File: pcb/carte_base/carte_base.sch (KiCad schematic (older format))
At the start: 40 parts, among them J1 Conn_01x04, J2 Conn_01x02, J3 Conn_01x02, J4 Conn_01x02, SW1 FSMRA3JH04, U1 STM32L031, U2 DAC7563T, U3 TS9222IDT

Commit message: Carte base finie
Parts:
- removed R10, R11, R12, R13, R8, R9: 1K, Resistor_SMD:R_1206_3216Metric_Pad1.42x1.75mm_HandSolder, symbol Device:R
- removed U2: DAC7563T, Package_SO:VSSOP-10_3x3mm_P0.5mm, symbol Insa:DAC7563T
- removed U3: TS9222IDT, Package_SO:SO-8_3.9x4.9mm_P1.27mm, symbol Insa:TS9222IDT
- added C15, C16, C17, C18: 22nF, Capacitor_SMD:C_1206_3216Metric_Pad1.42x1.75mm_HandSolder, symbol Device:C
- added J5: Conn_01x02, Insa:DF3A-2P-2DS, symbol Connector_Generic:Conn_01x02
- added RN1, RN3: 1K, Resistor_SMD:R_Array_Convex_4x1206, symbol Device:R_Pack04
- added RN2: 100, Resistor_SMD:R_Array_Convex_4x1206, symbol Device:R_Pack04
- added RN4: 2.4K, Resistor_SMD:R_Array_Convex_4x1206, symbol Device:R_Pack04
- added U2: DAC7554, Package_SO:MSOP-10_3x3mm_P0.5mm, symbol Insa:DAC7554
- added U3: TS9224IDT, Package_SO:SOIC-14_3.9x8.7mm_P1.27mm, symbol Insa:TS9224IDT
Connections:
- net labels added: 10V_Inclinaison_Pos, 10V_Inclinaison_VA, 10V_Rotation_Pos, 10V_Rotation_VA, Consigne_10V_Arriere, Consigne_10V_Avant, Vdrive
- net labels removed: Analog_12V_Inclinaison, Analog_12V_Rotation, Consigne_12V_Arriere, Consigne_12V_Avant, ~DAC_CLEAR
- wire segments 129 -> 184
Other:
- note added: "Connectique"
- note added: "Entrées analogiques et mise à l'echelle (0-3,3V)"
- note added: "Filtrage alimentation"
- note added: "Nucleo-L031"
- note added: "Sorties analogiques et mise à l'echelle (0-10V)"
- moved on the sheet: C1, C13, C14, C2, C3, C7, C8, D1, J1, J2, J3, J4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

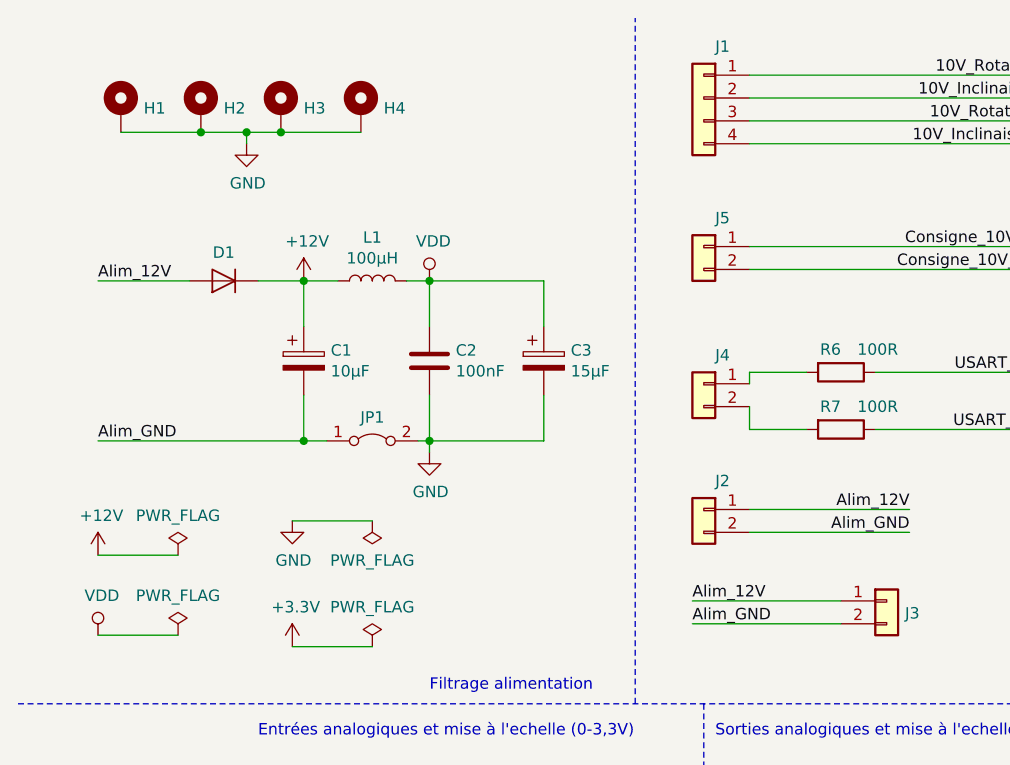
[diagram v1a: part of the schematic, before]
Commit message: Correction sur carte base
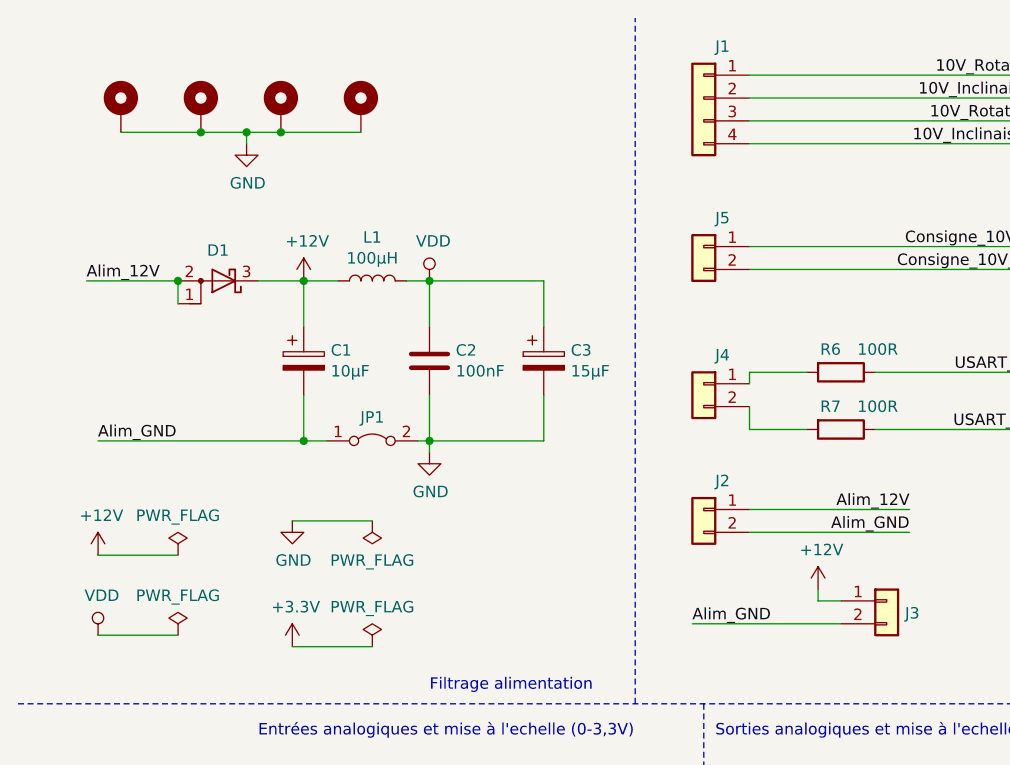
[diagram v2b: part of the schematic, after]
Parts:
- removed D1: D, Diode_SMD:D_SOD-123, symbol Device:D
- added D1: D_Schottky_AAK, Package_TO_SOT_SMD:TO-277A, symbol Device:D_Schottky_AAK
- RN1, RN2, RN3, RN4: footprint Resistor_SMD:R_Array_Convex_4x1206 -> Resistor_SMD:R_Array_Convex_4x0603
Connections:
- net +12V: now also J3.1 (Pin_1), D1.3 (K)
- net Alim_12V: now also D1.1 (A), D1.2 (A); no longer J3.1 (Pin_1)
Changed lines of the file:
@@
 U 1 1 5D2F2658
 P 950 900
-F 0 "H1" H 1050 905 50  0000 L CNN
+F 0 "H1" H 1050 905 50  0001 L CNN
 F 1 "MountingHole_Pad" H 1050 860 50  0001 L CNN
 F 2 "MountingHole:MountingHole_3.2mm_M3_ISO14580_Pad" H 950 900 50  0001 C CNN
@@
 U 1 1 5D2F26FB
 P 1300 900
-F 0 "H2" H 1400 905 50  0000 L CNN
+F 0 "H2" H 1400 905 50  0001 L CNN
 F 1 "MountingHole_Pad" H 1400 860 50  0001 L CNN
 F 2 "MountingHole:MountingHole_3.2mm_M3_ISO14580_Pad" H 1300 900 50  0001 C CNN
@@
 U 1 1 5D2F2813
 P 1650 900
-F 0 "H3" H 1750 905 50  0000 L CNN
+F 0 "H3" H 1750 905 50  0001 L CNN
 F 1 "MountingHole_Pad" H 1750 860 50  0001 L CNN
 F 2 "MountingHole:MountingHole_3.2mm_M3_ISO14580_Pad" H 1650 900 50  0001 C CNN
@@
 U 1 1 5D2F288E
 P 2000 900
-F 0 "H4" H 2100 905 50  0000 L CNN
+F 0 "H4" H 2100 905 50  0001 L CNN
 F 1 "MountingHole_Pad" H 2100 860 50  0001 L CNN
 F 2 "MountingHole:MountingHole_3.2mm_M3_ISO14580_Pad" H 2000 900 50  0001 C CNN
@@
 $EndComp
 Connection ~ 2300 1650
-Text Label 850  1650 0    50   ~ 0
+Text Label 800  1650 0    50   ~ 0
 Alim_12V
 Text Label 850  2350 0    50   ~ 0
@@
 $EndComp
 $Comp
-L Device:D D1
-U 1 1 5D8D967B
-P 1400 1650
-F 0 "D1" H 1400 1526 50  0000 C CNN
-F 1 "D" H 1400 1525 50  0001 C CNN
-F 2 "Diode_SMD:D_SOD-123" H 1400 1650 50  0001 C CNN
-F 3 "~" H 1400 1650 50  0001 C CNN
-	1    1400 1650
-	-1   0    0    1
-$EndComp
-$Comp
 L Device:CP C3
 U 1 1 5D8DE5DD
@@
 	1    0    0    -1
 $EndComp
-Wire Wire Line
-	3450 3050 4100 3050
-Text Label 3450 3050 0    50   ~ 0
-Alim_12V
 Wire Wire Line
 	4100 3150 3450 3150
@@
 DAC_DATA
 Wire Wire Line
-	1250 1650 850  1650
+	1200 1650 800  1650
 Wire Wire Line
 	1550 1650 1750 1650
@@
 F 0 "RN1" V 4883 4950 50  0000 C CNN
 F 1 "1K" V 4974 4950 50  0000 C CNN
-F 2 "Resistor_SMD:R_Array_Convex_4x1206" V 5575 4950 50  0001 C CNN
+F 2 "Resistor_SMD:R_Array_Convex_4x0603" V 5575 4950 50  0001 C CNN
 F 3 "~" H 5300 4950 50  0001 C CNN
 F 4 "CAY16-102J4AS" V 5300 4950 50  0001 C CNN "Ref"
@@
 F 0 "RN2" V 8983 5000 50  0000 C CNN
 F 1 "100" V 9074 5000 50  0000 C CNN
-F 2 "Resistor_SMD:R_Array_Convex_4x1206" V 9675 5000 50  0001 C CNN
+F 2 "Resistor_SMD:R_Array_Convex_4x0603" V 9675 5000 50  0001 C CNN
 F 3 "~" H 9400 5000 50  0001 C CNN
 F 4 "CAY16-101J4AS" V 9400 5000 50  0001 C CNN "Ref"
@@
 F 0 "RN3" H 6650 5850 50  0000 L CNN
 F 1 "1K" H 6700 5750 50  0000 L CNN
-F 2 "Resistor_SMD:R_Array_Convex_4x1206" V 7375 5750 50  0001 C CNN
+F 2 "Resistor_SMD:R_Array_Convex_4x0603" V 7375 5750 50  0001 C CNN
 F 3 "~" H 7100 5750 50  0001 C CNN
 F 4 "CAY16-102J4AS" V 7100 5750 50  0001 C CNN "Ref"
@@
 F 0 "RN4" V 8200 6150 50  0000 C CNN
 F 1 "2.4K" V 8300 6150 50  0000 C CNN
-F 2 "Resistor_SMD:R_Array_Convex_4x1206" V 8275 6150 50  0001 C CNN
+F 2 "Resistor_SMD:R_Array_Convex_4x0603" V 8275 6150 50  0001 C CNN
 F 3 "~" H 8000 6150 50  0001 C CNN
 F 4 "YC164-FR-072K4L" V 8000 6150 50  0001 C CNN "Ref"
@@
 Wire Wire Line
 	7450 4450 7550 4450
+$Comp
+L power:+12V #PWR0130
+U 1 1 5D9C510B
+P 4000 3000
+F 0 "#PWR0130" H 4000 2850 50  0001 C CNN
+F 1 "+12V" H 4015 3173 50  0000 C CNN
+F 2 "" H 4000 3000 50  0001 C CNN
+F 3 "" H 4000 3000 50  0001 C CNN
+	1    4000 3000
+	1    0    0    -1
+$EndComp
+Wire Wire Line
+	4100 3050 4000 3050
+Wire Wire Line
+	4000 3050 4000 3000
+$Comp
+L Device:D_Schottky_AAK D1
+U 1 1 5D9FB932
+P 1400 1650
+F 0 "D1" H 1425 1517 50  0000 C CNN
+F 1 "D_Schottky_AAK" H 1425 1516 50  0001 C CNN
+F 2 "Package_TO_SOT_SMD:TO-277A" H 1400 1650 50  0001 C CNN
+F 3 "~" H 1400 1650 50  0001 C CNN
+	1    1400 1650
+	-1   0    0    1
+$EndComp
+Wire Wire Line
+	1200 1750 1200 1650
+Connection ~ 1200 1650
 $EndSCHEMATC

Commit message: petites evolutions sur PCB
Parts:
- D1: Ref (none) -> SS10P4C-M3/86A
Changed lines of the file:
@@
 F 2 "Package_TO_SOT_SMD:TO-277A" H 1400 1650 50  0001 C CNN
 F 3 "~" H 1400 1650 50  0001 C CNN
+F 4 "SS10P4C-M3/86A" H 1400 1650 50  0001 C CNN "Ref"
 	1    1400 1650
 	-1   0    0    1

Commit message: creation du projet logiciel Helicoptere_embarque
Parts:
- D1: symbol Device:D_Schottky_AAK -> carte_base-rescue:D_Schottky_AAK-Device
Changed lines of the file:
@@
 	4000 3050 4000 3000
 $Comp
-L Device:D_Schottky_AAK D1
+L carte_base-rescue:D_Schottky_AAK-Device D1
 U 1 1 5D9FB932
 P 1400 1650
